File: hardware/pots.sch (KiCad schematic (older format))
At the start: 40 parts, among them SW1 Switch_SW_Push, SW2 Switch_SW_Push, SW3 Switch_SW_Push, SW4 Switch_SW_Push, U4 4067, U5 TLC5947DAP

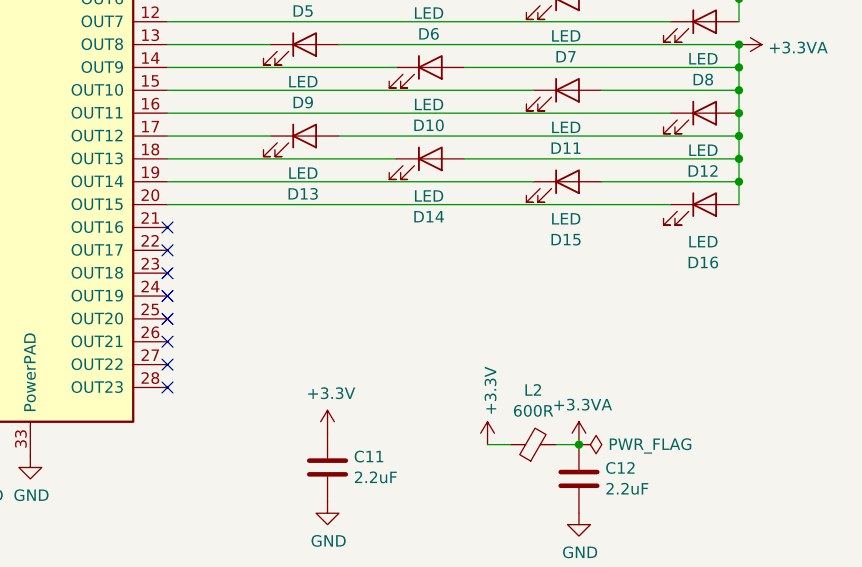
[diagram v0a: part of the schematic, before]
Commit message: try to fix the wiring a bit, signal integrity might be an issue with 2 layer and teensy breakout
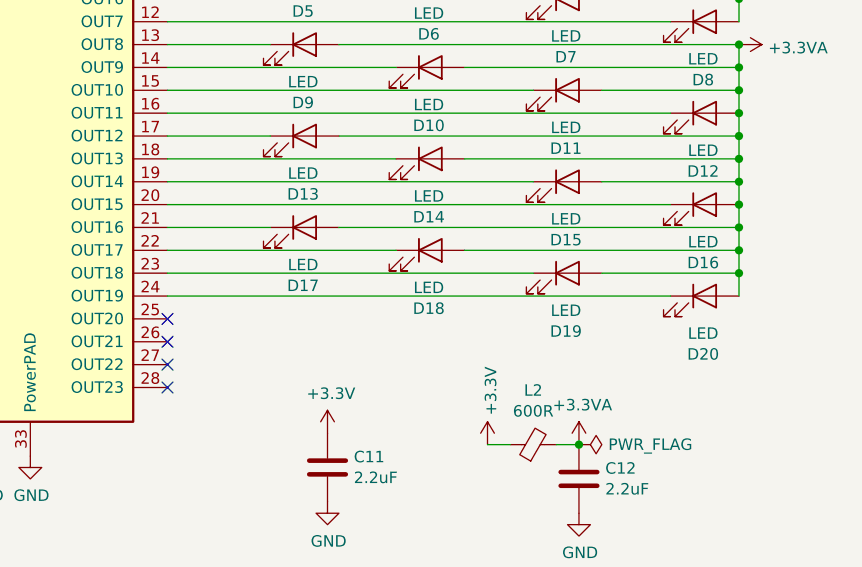
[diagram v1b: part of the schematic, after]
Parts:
- added D17, D18, D19, D20: LED, LED_SMD:LED_0805_2012Metric, symbol Device:LED
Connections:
- net +3.3VA: now also D17.2 (A), D18.2 (A), D19.2 (A), D20.2 (A)
- net at U5.21 (OUT16): now also D17.1 (K)
- net at U5.22 (OUT17): now also D18.1 (K)
- net at U5.23 (OUT18): now also D19.1 (K)
- net at U5.24 (OUT19): now also D20.1 (K)
- no-connect marks 13 -> 9
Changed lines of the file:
@@
 	1    0    0    -1
 $EndComp
-NoConn ~ 7650 4000
-NoConn ~ 7650 4100
-NoConn ~ 7650 4200
-NoConn ~ 7650 4300
 NoConn ~ 7650 4400
 NoConn ~ 7650 4500
@@
 Wire Notes Line
 	2600 3900 800  3900
+$Comp
+L Device:LED D19
+U 1 1 5E0F956E
+P 9400 4200
+F 0 "D19" H 9393 3945 50  0000 C CNN
+F 1 "LED" H 9393 4036 50  0000 C CNN
+F 2 "LED_SMD:LED_0805_2012Metric" H 9400 4200 50  0001 C CNN
+F 3 "~" H 9400 4200 50  0001 C CNN
+	1    9400 4200
+	1    0    0    -1
+$EndComp
+$Comp
+L Device:LED D18
+U 1 1 5E0F9578
+P 8800 4100
+F 0 "D18" H 8793 3845 50  0000 C CNN
+F 1 "LED" H 8793 3936 50  0000 C CNN
+F 2 "LED_SMD:LED_0805_2012Metric" H 8800 4100 50  0001 C CNN
+F 3 "~" H 8800 4100 50  0001 C CNN
+	1    8800 4100
+	1    0    0    -1
+$EndComp
+$Comp
+L Device:LED D17
+U 1 1 5E0F9582
+P 8250 4000
+F 0 "D17" H 8243 3745 50  0000 C CNN
+F 1 "LED" H 8243 3836 50  0000 C CNN
+F 2 "LED_SMD:LED_0805_2012Metric" H 8250 4000 50  0001 C CNN
+F 3 "~" H 8250 4000 50  0001 C CNN
+	1    8250 4000
+	1    0    0    -1
+$EndComp
+Wire Wire Line
+	7650 4000 8100 4000
+Wire Wire Line
+	8650 4100 7650 4100
+Wire Wire Line
+	7650 4200 9250 4200
+Wire Wire Line
+	9850 4300 7650 4300
+Wire Wire Line
+	8400 4000 10150 4000
+Wire Wire Line
+	8950 4100 10150 4100
+Wire Wire Line
+	9550 4200 10150 4200
+$Comp
+L Device:LED D20
+U 1 1 5E0F959D
+P 10000 4300
+F 0 "D20" H 9993 4045 50  0000 C CNN
+F 1 "LED" H 9993 4136 50  0000 C CNN
+F 2 "LED_SMD:LED_0805_2012Metric" H 10000 4300 50  0001 C CNN
+F 3 "~" H 10000 4300 50  0001 C CNN
+	1    10000 4300
+	1    0    0    -1
+$EndComp
+Wire Wire Line
+	10150 4300 10150 4200
+Connection ~ 10150 3900
+Connection ~ 10150 4000
+Wire Wire Line
+	10150 4000 10150 3900
+Connection ~ 10150 4100
+Wire Wire Line
+	10150 4100 10150 4000
+Connection ~ 10150 4200
+Wire Wire Line
+	10150 4200 10150 4100
 $EndSCHEMATC

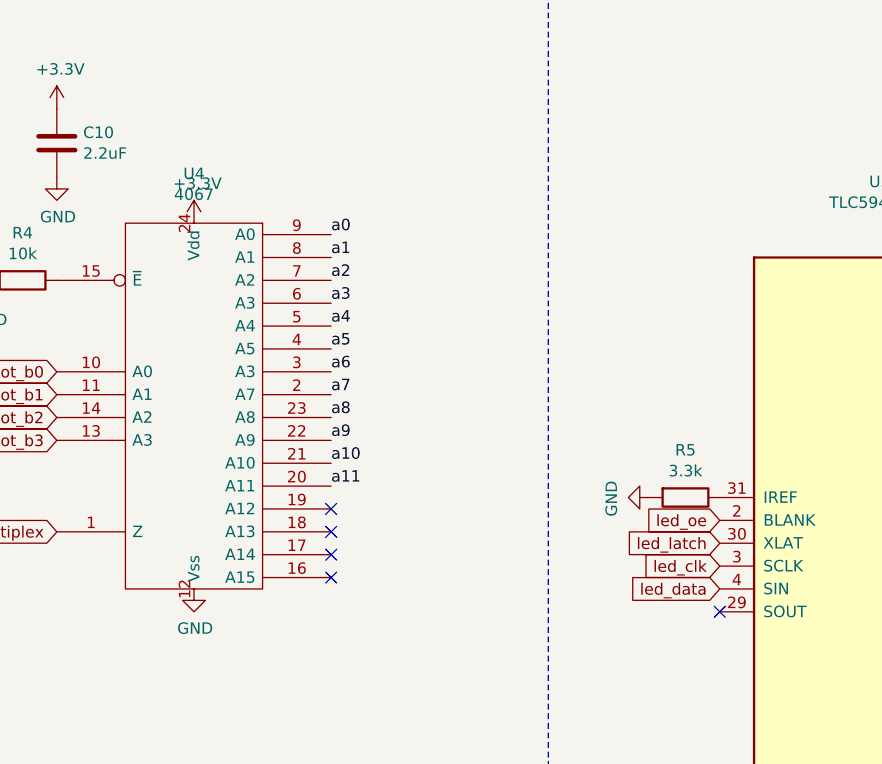
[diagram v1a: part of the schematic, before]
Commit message: move to 4 layer board, change size for cost, add optional flash
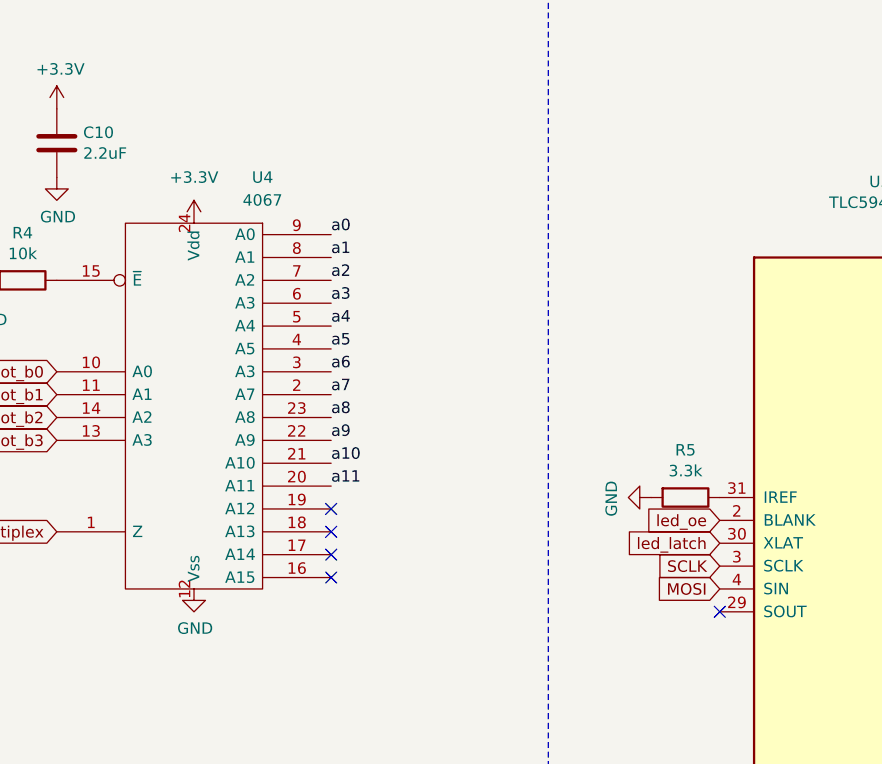
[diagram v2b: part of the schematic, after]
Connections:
- net led_clk renamed SCLK
- net led_data renamed MOSI
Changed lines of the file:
@@
 P 3950 2100
 F 0 "#PWR0148" H 3950 1950 50  0001 C CNN
-F 1 "+3.3V" H 3965 2273 50  0000 C CNN
+F 1 "+3.3V" H 3950 2300 50  0000 C CNN
 F 2 "" H 3950 2100 50  0001 C CNN
 F 3 "" H 3950 2100 50  0001 C CNN
@@
 U 1 1 5E1AC48F
 P 3950 2900
-F 0 "U4" H 3950 3916 50  0000 C CNN
-F 1 "4067" H 3950 3825 50  0000 C CNN
+F 0 "U4" H 4250 3900 50  0000 C CNN
+F 1 "4067" H 4250 3800 50  0000 C CNN
 F 2 "Package_SO:SSOP-24_5.3x8.2mm_P0.65mm" H 3950 2900 50  0001 C CNN
 F 3 "https://www.ti.com/lit/ds/symlink/cd74hc4067.pdf" H 3950 2900 50  0001 C CNN
@@
 led_oe
 Text GLabel 6250 3600 0    50   Input ~ 0
-led_clk
+SCLK
 Text GLabel 6250 3700 0    50   Input ~ 0
-led_data
+MOSI
 Text GLabel 6250 3500 0    50   Input ~ 0
 led_latch

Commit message: change 3v3 plane to gnd, route all i2s signals on top plane, add rc filter for ADC pot input
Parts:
- added C16: 2.2uF, Capacitor_SMD:C_0805_2012Metric, symbol Device:C
- added R10: 200r, Resistor_SMD:R_0805_2012Metric, symbol Device:R
- SW1, SW2, SW3, SW4: symbol teensy_beats-cache:Switch_SW_Push -> teensy-fx-rescue:Switch_SW_Push-teensy_beats-cache
- U4: symbol teensy_beats-cache:4067 -> teensy-fx-rescue:4067-teensy_beats-cache
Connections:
- net GND: now also C16.2
- net pot_multiplex: now also C16.1, R10.2; no longer U4.1 (Z)
- new net: R10.1, U4.1 (Z)
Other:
- note added: "RC filter\n200R & 2.2u = 360Hz cutoff"
- moved on the sheet: C10, R4, U4
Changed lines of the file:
@@
 L Device:R R4
 U 1 1 5E17A27D
-P 3200 2350
-F 0 "R4" V 2993 2350 50  0000 C CNN
-F 1 "10k" V 3084 2350 50  0000 C CNN
-F 2 "Resistor_SMD:R_0805_2012Metric" V 3130 2350 50  0001 C CNN
-F 3 "~" H 3200 2350 50  0001 C CNN
-	1    3200 2350
+P 3450 2300
+F 0 "R4" V 3243 2300 50  0000 C CNN
+F 1 "10k" V 3334 2300 50  0000 C CNN
+F 2 "Resistor_SMD:R_0805_2012Metric" V 3380 2300 50  0001 C CNN
+F 3 "~" H 3450 2300 50  0001 C CNN
+	1    3450 2300
 	0    1    1    0
 $EndComp
@@
 L power:GND #PWR0121
 U 1 1 5E17AA89
-P 3050 2350
-F 0 "#PWR0121" H 3050 2100 50  0001 C CNN
-F 1 "GND" H 3055 2177 50  0000 C CNN
-F 2 "" H 3050 2350 50  0001 C CNN
-F 3 "" H 3050 2350 50  0001 C CNN
-	1    3050 2350
-	1    0    0    -1
-$EndComp
-Text GLabel 3350 3450 0    50   Input ~ 0
+P 3300 2300
+F 0 "#PWR0121" H 3300 2050 50  0001 C CNN
+F 1 "GND" H 3305 2127 50  0000 C CNN
+F 2 "" H 3300 2300 50  0001 C CNN
+F 3 "" H 3300 2300 50  0001 C CNN
+	1    3300 2300
+	1    0    0    -1
+$EndComp
+Text GLabel 3250 3400 0    50   Input ~ 0
 pot_multiplex
-Text GLabel 3350 2750 0    50   Input ~ 0
+Text GLabel 3600 2700 0    50   Input ~ 0
 pot_b0
-Text GLabel 3350 2850 0    50   Input ~ 0
+Text GLabel 3600 2800 0    50   Input ~ 0
 pot_b1
-Text GLabel 3350 2950 0    50   Input ~ 0
+Text GLabel 3600 2900 0    50   Input ~ 0
 pot_b2
-Text GLabel 3350 3050 0    50   Input ~ 0
+Text GLabel 3600 3000 0    50   Input ~ 0
 pot_b3
 $Comp
@@
 Text Label 1800 4900 0    50   ~ 0
 a0
-Text Label 4550 2150 0    50   ~ 0
+Text Label 4800 2100 0    50   ~ 0
 a0
-Text Label 4550 2250 0    50   ~ 0
+Text Label 4800 2200 0    50   ~ 0
 a1
-Text Label 4550 2350 0    50   ~ 0
+Text Label 4800 2300 0    50   ~ 0
 a2
-Text Label 4550 2450 0    50   ~ 0
+Text Label 4800 2400 0    50   ~ 0
 a3
-Text Label 4550 2550 0    50   ~ 0
+Text Label 4800 2500 0    50   ~ 0
 a4
-Text Label 4550 2650 0    50   ~ 0
+Text Label 4800 2600 0    50   ~ 0
 a5
-Text Label 4550 2750 0    50   ~ 0
+Text Label 4800 2700 0    50   ~ 0
 a6
-Text Label 4550 2850 0    50   ~ 0
+Text Label 4800 2800 0    50   ~ 0
 a7
-Text Label 4550 2950 0    50   ~ 0
+Text Label 4800 2900 0    50   ~ 0
 a8
-Text Label 4550 3050 0    50   ~ 0
+Text Label 4800 3000 0    50   ~ 0
 a9
-Text Label 4550 3150 0    50   ~ 0
+Text Label 4800 3100 0    50   ~ 0
 a10
-Text Label 4550 3250 0    50   ~ 0
+Text Label 4800 3200 0    50   ~ 0
 a11
 $Comp
@@
 L power:GND #PWR0147
 U 1 1 5E1946A6
-P 3950 3700
-F 0 "#PWR0147" H 3950 3450 50  0001 C CNN
-F 1 "GND" H 3955 3527 50  0000 C CNN
-F 2 "" H 3950 3700 50  0001 C CNN
-F 3 "" H 3950 3700 50  0001 C CNN
-	1    3950 3700
+P 4200 3650
+F 0 "#PWR0147" H 4200 3400 50  0001 C CNN
+F 1 "GND" H 4205 3477 50  0000 C CNN
+F 2 "" H 4200 3650 50  0001 C CNN
+F 3 "" H 4200 3650 50  0001 C CNN
+	1    4200 3650
 	1    0    0    -1
 $EndComp
@@
 L power:+3.3V #PWR0148
 U 1 1 5E194A9C
-P 3950 2100
-F 0 "#PWR0148" H 3950 1950 50  0001 C CNN
-F 1 "+3.3V" H 3950 2300 50  0000 C CNN
-F 2 "" H 3950 2100 50  0001 C CNN
-F 3 "" H 3950 2100 50  0001 C CNN
-	1    3950 2100
-	1    0    0    -1
-$EndComp
-$Comp
-L teensy_beats-cache:4067 U4
+P 4200 2050
+F 0 "#PWR0148" H 4200 1900 50  0001 C CNN
+F 1 "+3.3V" H 4200 2250 50  0000 C CNN
+F 2 "" H 4200 2050 50  0001 C CNN
+F 3 "" H 4200 2050 50  0001 C CNN
+	1    4200 2050
+	1    0    0    -1
+$EndComp
+$Comp
+L teensy-fx-rescue:4067-teensy_beats-cache U4
 U 1 1 5E1AC48F
-P 3950 2900
-F 0 "U4" H 4250 3900 50  0000 C CNN
-F 1 "4067" H 4250 3800 50  0000 C CNN
-F 2 "Package_SO:SSOP-24_5.3x8.2mm_P0.65mm" H 3950 2900 50  0001 C CNN
-F 3 "https://www.ti.com/lit/ds/symlink/cd74hc4067.pdf" H 3950 2900 50  0001 C CNN
-	1    3950 2900
+P 4200 2850
+AR Path="/5E1AC48F" Ref="U4"  Part="1"
+AR Path="/5E177B2B/5E1AC48F" Ref="U4"  Part="1"
+F 0 "U4" H 4500 3850 50  0000 C CNN
+F 1 "4067" H 4500 3750 50  0000 C CNN
+F 2 "Package_SO:SSOP-24_5.3x8.2mm_P0.65mm" H 4200 2850 50  0001 C CNN
+F 3 "https://www.ti.com/lit/ds/symlink/cd74hc4067.pdf" H 4200 2850 50  0001 C CNN
+	1    4200 2850
 	1    0    0    -1
 $EndComp
@@
 L Device:C C10
 U 1 1 5E1AEABA
-P 3350 1750
-F 0 "C10" H 3465 1796 50  0000 L CNN
-F 1 "2.2uF" H 3465 1705 50  0000 L CNN
-F 2 "Capacitor_SMD:C_0805_2012Metric" H 3388 1600 50  0001 C CNN
-F 3 "~" H 3350 1750 50  0001 C CNN
-	1    3350 1750
+P 3600 1700
+F 0 "C10" H 3715 1746 50  0000 L CNN
+F 1 "2.2uF" H 3715 1655 50  0000 L CNN
+F 2 "Capacitor_SMD:C_0805_2012Metric" H 3638 1550 50  0001 C CNN
+F 3 "~" H 3600 1700 50  0001 C CNN
+	1    3600 1700
 	1    0    0    -1
 $EndComp
@@
 L power:+3.3V #PWR0149
 U 1 1 5E1AF1C5
-P 3350 1600
-F 0 "#PWR0149" H 3350 1450 50  0001 C CNN
-F 1 "+3.3V" H 3365 1773 50  0000 C CNN
-F 2 "" H 3350 1600 50  0001 C CNN
-F 3 "" H 3350 1600 50  0001 C CNN
-	1    3350 1600
+P 3600 1550
+F 0 "#PWR0149" H 3600 1400 50  0001 C CNN
+F 1 "+3.3V" H 3615 1723 50  0000 C CNN
+F 2 "" H 3600 1550 50  0001 C CNN
+F 3 "" H 3600 1550 50  0001 C CNN
+	1    3600 1550
 	1    0    0    -1
 $EndComp
@@
 L power:GND #PWR0150
 U 1 1 5E1AF422
-P 3350 1900
-F 0 "#PWR0150" H 3350 1650 50  0001 C CNN
-F 1 "GND" H 3355 1727 50  0000 C CNN
-F 2 "" H 3350 1900 50  0001 C CNN
-F 3 "" H 3350 1900 50  0001 C CNN
-	1    3350 1900
+P 3600 1850
+F 0 "#PWR0150" H 3600 1600 50  0001 C CNN
+F 1 "GND" H 3605 1677 50  0000 C CNN
+F 2 "" H 3600 1850 50  0001 C CNN
+F 3 "" H 3600 1850 50  0001 C CNN
+	1    3600 1850
 	1    0    0    -1
 $EndComp
@@
 $EndComp
 $Comp
-L teensy_beats-cache:Switch_SW_Push SW1
+L teensy-fx-rescue:Switch_SW_Push-teensy_beats-cache SW1
 U 1 1 5E252246
 P 1600 2150
+AR Path="/5E252246" Ref="SW1"  Part="1"
+AR Path="/5E177B2B/5E252246" Ref="SW1"  Part="1"
 F 0 "SW1" H 1600 2435 50  0000 C CNN
 F 1 "Switch_SW_Push" H 1600 2344 50  0000 C CNN
@@
 $EndComp
 $Comp
-L teensy_beats-cache:Switch_SW_Push SW2
+L teensy-fx-rescue:Switch_SW_Push-teensy_beats-cache SW2
 U 1 1 5E252D7C
 P 1600 2600
+AR Path="/5E252D7C" Ref="SW2"  Part="1"
+AR Path="/5E177B2B/5E252D7C" Ref="SW2"  Part="1"
 F 0 "SW2" H 1600 2885 50  0000 C CNN
 F 1 "Switch_SW_Push" H 1600 2794 50  0000 C CNN
@@
 $EndComp
 $Comp
-L teensy_beats-cache:Switch_SW_Push SW3
+L teensy-fx-rescue:Switch_SW_Push-teensy_beats-cache SW3
 U 1 1 5E2538C8
 P 1600 3000
+AR Path="/5E2538C8" Ref="SW3"  Part="1"
+AR Path="/5E177B2B/5E2538C8" Ref="SW3"  Part="1"
 F 0 "SW3" H 1600 3285 50  0000 C CNN
 F 1 "Switch_SW_Push" H 1600 3194 50  0000 C CNN
@@
 $EndComp
 $Comp
-L teensy_beats-cache:Switch_SW_Push SW4
+L teensy-fx-rescue:Switch_SW_Push-teensy_beats-cache SW4
 U 1 1 5E253CCE
 P 1600 3400
+AR Path="/5E253CCE" Ref="SW4"  Part="1"
+AR Path="/5E177B2B/5E253CCE" Ref="SW4"  Part="1"
 F 0 "SW4" H 1600 3685 50  0000 C CNN
 F 1 "Switch_SW_Push" H 1600 3594 50  0000 C CNN
@@
 	0    -1   -1   0
 $EndComp
-NoConn ~ 4550 3350
-NoConn ~ 4550 3450
-NoConn ~ 4550 3550
-NoConn ~ 4550 3650
+NoConn ~ 4800 3300
+NoConn ~ 4800 3400
+NoConn ~ 4800 3500
+NoConn ~ 4800 3600
 $Comp
 L Device:LED D7
@@
 Wire Wire Line
 	10150 4200 10150 4100
+$Comp
+L Device:R R10
+U 1 1 5E14FB1F
+P 3450 3400
+F 0 "R10" V 3243 3400 50  0000 C CNN
+F 1 "200r" V 3334 3400 50  0000 C CNN
+F 2 "Resistor_SMD:R_0805_2012Metric" V 3380 3400 50  0001 C CNN
+F 3 "~" H 3450 3400 50  0001 C CNN
+	1    3450 3400
+	0    1    1    0
+$EndComp
+$Comp
+L Device:C C16
+U 1 1 5E1525F8
+P 3300 3550
+F 0 "C16" H 3415 3596 50  0000 L CNN
+F 1 "2.2uF" H 3415 3505 50  0000 L CNN
+F 2 "Capacitor_SMD:C_0805_2012Metric" H 3338 3400 50  0001 C CNN
+F 3 "~" H 3300 3550 50  0001 C CNN
+	1    3300 3550
+	1    0    0    -1
+$EndComp
+$Comp
+L power:GND #PWR0177
+U 1 1 5E1577D0
+P 3300 3700
+F 0 "#PWR0177" H 3300 3450 50  0001 C CNN
+F 1 "GND" H 3305 3527 50  0000 C CNN
+F 2 "" H 3300 3700 50  0001 C CNN
+F 3 "" H 3300 3700 50  0001 C CNN
+	1    3300 3700
+	1    0    0    -1
+$EndComp
+Wire Wire Line
+	3250 3400 3300 3400
+Connection ~ 3300 3400
+Text Notes 2800 4150 0    50   ~ 0
+RC filter\n200R & 2.2u = 360Hz cutoff
 $EndSCHEMATC

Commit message: notes, check current, add extra decoupling cap for reg, move led supply to 5v
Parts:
- R5: value 3.3k -> 5k
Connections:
- net +3V3: no longer L2.1
- net +3.3VA renamed +5VA
- new net +5V: L2.1
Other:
- note added: "R5 is 5k to set LED current to 10mA\nVLED > LED VF + 0.4v"
- note added: "all pots 10k, taper 1b (linear)"
- note added: "all pots together = 4mA"
- moved on the sheet: C11
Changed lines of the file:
@@
 U 1 1 5E0F221D
 P 6950 3600
-F 0 "U5" H 6950 5281 50  0000 C CNN
-F 1 "TLC5947DAP" H 6950 5190 50  0000 C CNN
+F 0 "U5" H 6850 5300 50  0000 C CNN
+F 1 "TLC5947DAP" H 6850 5200 50  0000 C CNN
 F 2 "Package_SO:HTSSOP-32-1EP_6.1x11mm_P0.65mm_EP5.2x11mm_Mask4.11x4.36mm" H 6400 5200 50  0001 L CNN
 F 3 "http://www.ti.com/lit/ds/symlink/tlc5947.pdf" H 6950 3600 50  0001 C CNN
@@
 	9850 3100 7650 3100
 Wire Wire Line
-	10150 3100 10150 3000
-Wire Wire Line
 	10150 2400 8400 2400
 Connection ~ 10150 2700
@@
 Wire Wire Line
 	10150 3000 10150 2900
-$Comp
-L power:+3.3VA #PWR0151
-U 1 1 5E15643A
-P 10150 2400
-F 0 "#PWR0151" H 10150 2250 50  0001 C CNN
-F 1 "+3.3VA" V 10165 2528 50  0000 L CNN
-F 2 "" H 10150 2400 50  0001 C CNN
-F 3 "" H 10150 2400 50  0001 C CNN
-	1    10150 2400
-	0    1    1    0
-$EndComp
-Connection ~ 10150 2400
 $Comp
 L Device:LED D8
@@
 	10150 3800 10150 3700
 $Comp
-L power:+3.3VA #PWR0152
-U 1 1 5E1669D8
-P 10150 3200
-F 0 "#PWR0152" H 10150 3050 50  0001 C CNN
-F 1 "+3.3VA" V 10165 3328 50  0000 L CNN
-F 2 "" H 10150 3200 50  0001 C CNN
-F 3 "" H 10150 3200 50  0001 C CNN
-	1    10150 3200
-	0    1    1    0
-$EndComp
-Connection ~ 10150 3200
-$Comp
 L Device:LED D16
 U 1 1 5E1669E3
@@
 P 6100 3300
 F 0 "R5" V 5893 3300 50  0000 C CNN
-F 1 "3.3k" V 5984 3300 50  0000 C CNN
+F 1 "5k" V 5984 3300 50  0000 C CNN
 F 2 "Resistor_SMD:R_0805_2012Metric" V 6030 3300 50  0001 C CNN
 F 3 "~" H 6100 3300 50  0001 C CNN
@@
 L Device:C C11
 U 1 1 5E19BB80
-P 8350 5050
-F 0 "C11" H 8465 5096 50  0000 L CNN
-F 1 "2.2uF" H 8465 5005 50  0000 L CNN
-F 2 "Capacitor_SMD:C_0805_2012Metric" H 8388 4900 50  0001 C CNN
-F 3 "~" H 8350 5050 50  0001 C CNN
-	1    8350 5050
+P 5850 2100
+F 0 "C11" H 5965 2146 50  0000 L CNN
+F 1 "2.2uF" H 5965 2055 50  0000 L CNN
+F 2 "Capacitor_SMD:C_0805_2012Metric" H 5888 1950 50  0001 C CNN
+F 3 "~" H 5850 2100 50  0001 C CNN
+	1    5850 2100
 	1    0    0    -1
 $EndComp
@@
 L power:+3.3V #PWR0157
 U 1 1 5E19BB8A
-P 8350 4900
-F 0 "#PWR0157" H 8350 4750 50  0001 C CNN
-F 1 "+3.3V" H 8365 5073 50  0000 C CNN
-F 2 "" H 8350 4900 50  0001 C CNN
-F 3 "" H 8350 4900 50  0001 C CNN
-	1    8350 4900
+P 5850 1950
+F 0 "#PWR0157" H 5850 1800 50  0001 C CNN
+F 1 "+3.3V" H 5865 2123 50  0000 C CNN
+F 2 "" H 5850 1950 50  0001 C CNN
+F 3 "" H 5850 1950 50  0001 C CNN
+	1    5850 1950
 	1    0    0    -1
 $EndComp
@@
 L power:GND #PWR0158
 U 1 1 5E19BB94
-P 8350 5200
-F 0 "#PWR0158" H 8350 4950 50  0001 C CNN
-F 1 "GND" H 8355 5027 50  0000 C CNN
-F 2 "" H 8350 5200 50  0001 C CNN
-F 3 "" H 8350 5200 50  0001 C CNN
-	1    8350 5200
+P 5850 2250
+F 0 "#PWR0158" H 5850 2000 50  0001 C CNN
+F 1 "GND" H 5855 2077 50  0000 C CNN
+F 2 "" H 5850 2250 50  0001 C CNN
+F 3 "" H 5850 2250 50  0001 C CNN
+	1    5850 2250
 	1    0    0    -1
 $EndComp
 NoConn ~ 6250 3800
-$Comp
-L power:+3.3VA #PWR0159
-U 1 1 5E1B6A2A
-P 9450 4950
-F 0 "#PWR0159" H 9450 4800 50  0001 C CNN
-F 1 "+3.3VA" H 9465 5123 50  0000 C CNN
-F 2 "" H 9450 4950 50  0001 C CNN
-F 3 "" H 9450 4950 50  0001 C CNN
-	1    9450 4950
-	1    0    0    -1
-$EndComp
-$Comp
-L power:+3.3V #PWR0160
-U 1 1 5E1B78CC
-P 9050 4950
-F 0 "#PWR0160" H 9050 4800 50  0001 C CNN
-F 1 "+3.3V" V 9065 5078 50  0000 L CNN
-F 2 "" H 9050 4950 50  0001 C CNN
-F 3 "" H 9050 4950 50  0001 C CNN
-	1    9050 4950
-	1    0    0    -1
-$EndComp
 $Comp
 L Device:C C12
@@
 Text Notes 2800 4150 0    50   ~ 0
 RC filter\n200R & 2.2u = 360Hz cutoff
+Text Notes 2200 7300 0    50   ~ 0
+all pots 10k, taper 1b (linear)
+Text Notes 2300 7450 0    50   ~ 0
+all pots together = 4mA
+Text Notes 7850 1350 0    50   ~ 0
+R5 is 5k to set LED current to 10mA\nVLED > LED VF + 0.4v
+$Comp
+L power:+5VA #PWR0151
+U 1 1 5E1803EC
+P 9450 4950
+F 0 "#PWR0151" H 9450 4800 50  0001 C CNN
+F 1 "+5VA" H 9465 5123 50  0000 C CNN
+F 2 "" H 9450 4950 50  0001 C CNN
+F 3 "" H 9450 4950 50  0001 C CNN
+	1    9450 4950
+	1    0    0    -1
+$EndComp
+$Comp
+L power:+5VA #PWR0152
+U 1 1 5E181433
+P 10150 2400
+F 0 "#PWR0152" H 10150 2250 50  0001 C CNN
+F 1 "+5VA" V 10165 2528 50  0000 L CNN
+F 2 "" H 10150 2400 50  0001 C CNN
+F 3 "" H 10150 2400 50  0001 C CNN
+	1    10150 2400
+	0    1    1    0
+$EndComp
+Connection ~ 10150 2400
+Wire Wire Line
+	10150 3000 10150 3100
+Connection ~ 10150 3200
+Connection ~ 10150 3100
+Wire Wire Line
+	10150 3100 10150 3200
+$Comp
+L power:+5V #PWR0159
+U 1 1 5E1903A9
+P 9050 4950
+F 0 "#PWR0159" H 9050 4800 50  0001 C CNN
+F 1 "+5V" H 9065 5123 50  0000 C CNN
+F 2 "" H 9050 4950 50  0001 C CNN
+F 3 "" H 9050 4950 50  0001 C CNN
+	1    9050 4950
+	1    0    0    -1
+$EndComp
 $EndSCHEMATC

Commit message: footprints
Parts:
- RV1: rs (none) -> 729-3600
- U4: farnell (none) -> 3124957
- U5: farnell (none) -> 1755259
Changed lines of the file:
@@
 F 1 "R_POT" H 1581 4855 50  0000 R CNN
 F 2 "audio-fx:Potentiometer_Alps_RK09L_Single_Vertical" H 1650 4900 50  0001 C CNN
-F 3 "https://www.alps.com/prod/info/E/PDF/Potentiometer/RotaryPotentiometers/RK09L/RK09L.pdf" H 1650 4900 50  0001 C CNN
+F 3 "https://docs.rs-online.com/06f8/0900766b80f4c571.pdf" H 1650 4900 50  0001 C CNN
+F 4 "" H 1650 4900 50  0001 C CNN "farnell"
+F 5 "729-3600" H 1650 4900 50  0001 C CNN "rs"
 	1    1650 4900
 	1    0    0    -1
@@
 F 2 "Package_SO:SSOP-24_5.3x8.2mm_P0.65mm" H 4200 2850 50  0001 C CNN
 F 3 "https://www.ti.com/lit/ds/symlink/cd74hc4067.pdf" H 4200 2850 50  0001 C CNN
+F 4 "3124957" H 4200 2850 50  0001 C CNN "farnell"
 	1    4200 2850
 	1    0    0    -1
@@
 F 2 "Package_SO:HTSSOP-32-1EP_6.1x11mm_P0.65mm_EP5.2x11mm_Mask4.11x4.36mm" H 6400 5200 50  0001 L CNN
 F 3 "http://www.ti.com/lit/ds/symlink/tlc5947.pdf" H 6950 3600 50  0001 C CNN
+F 4 "1755259" H 6950 3600 50  0001 C CNN "farnell"
 	1    6950 3600
 	1    0    0    -1
@@
 F 2 "Capacitor_SMD:C_0805_2012Metric" H 3338 3400 50  0001 C CNN
 F 3 "~" H 3300 3550 50  0001 C CNN
+F 4 "" H 3300 3550 50  0001 C CNN "farnell"
 	1    3300 3550
 	1    0    0    -1
